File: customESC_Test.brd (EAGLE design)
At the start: 152.4 x 127 mm, 54 parts

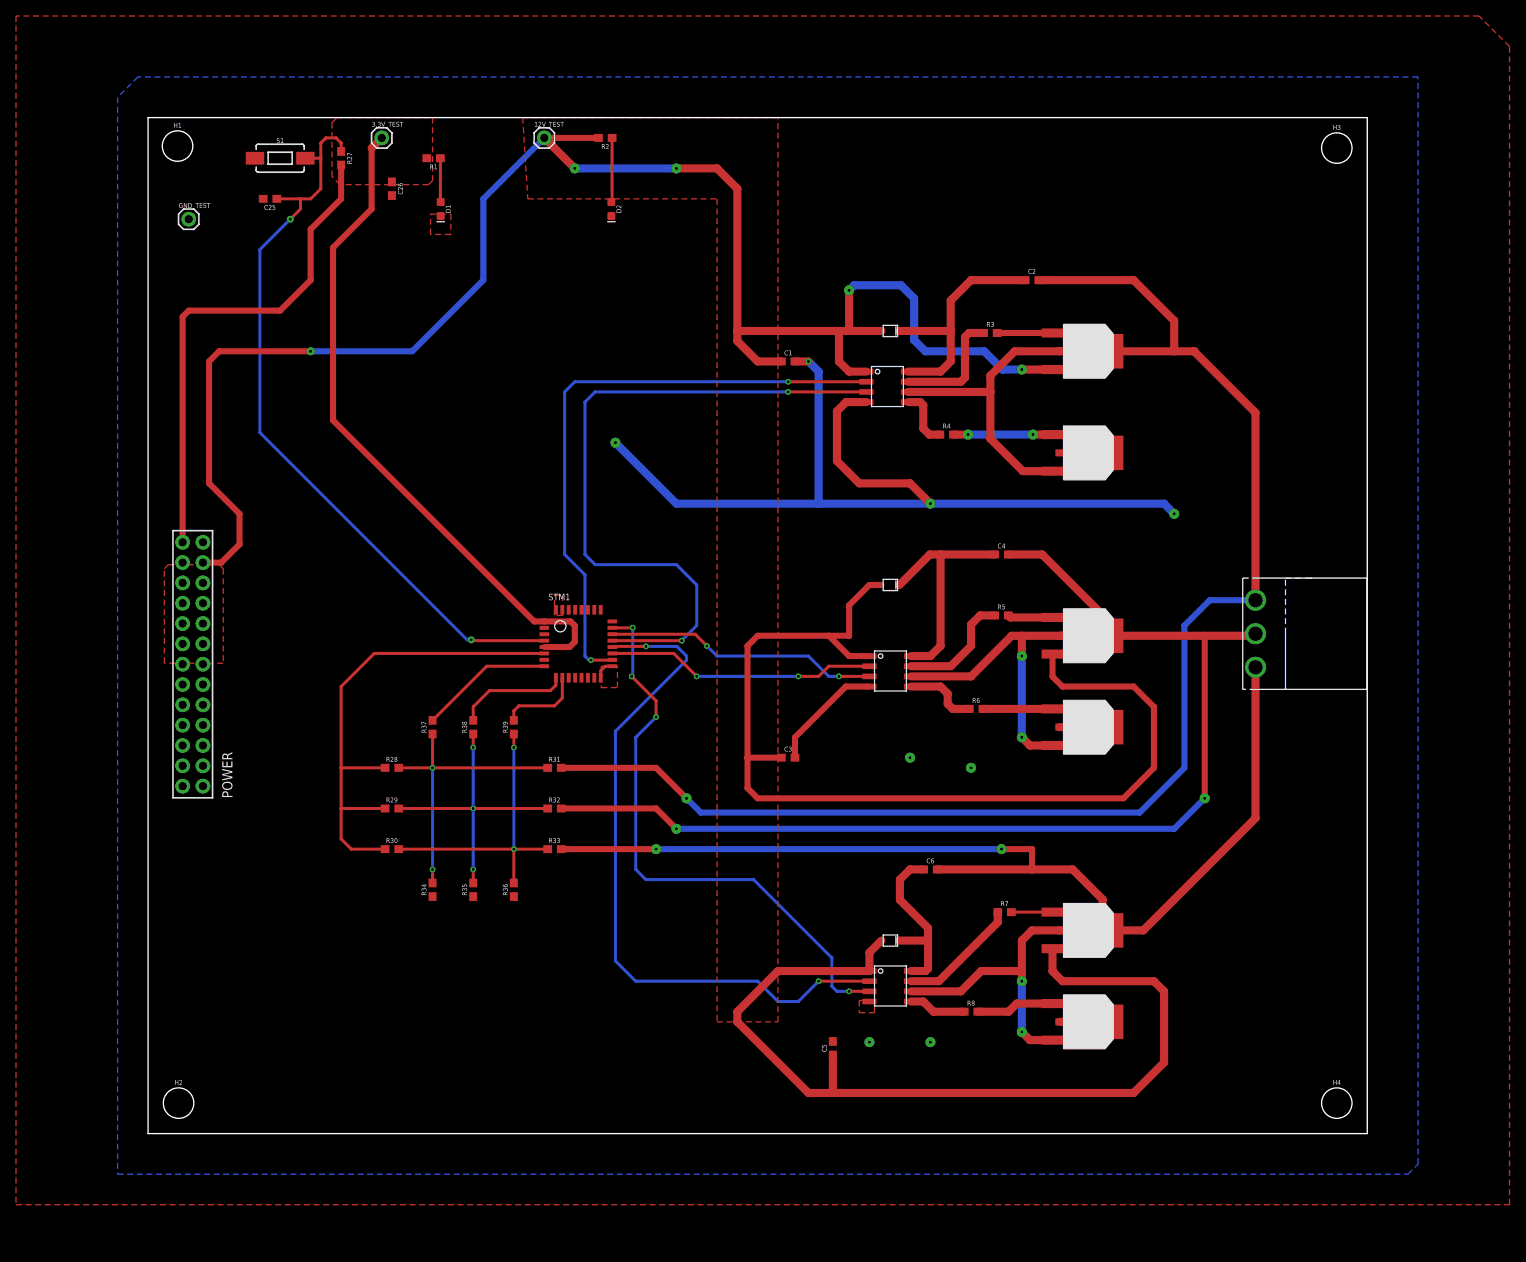
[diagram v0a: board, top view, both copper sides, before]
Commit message: added paths for input and added test leds. needs a design review
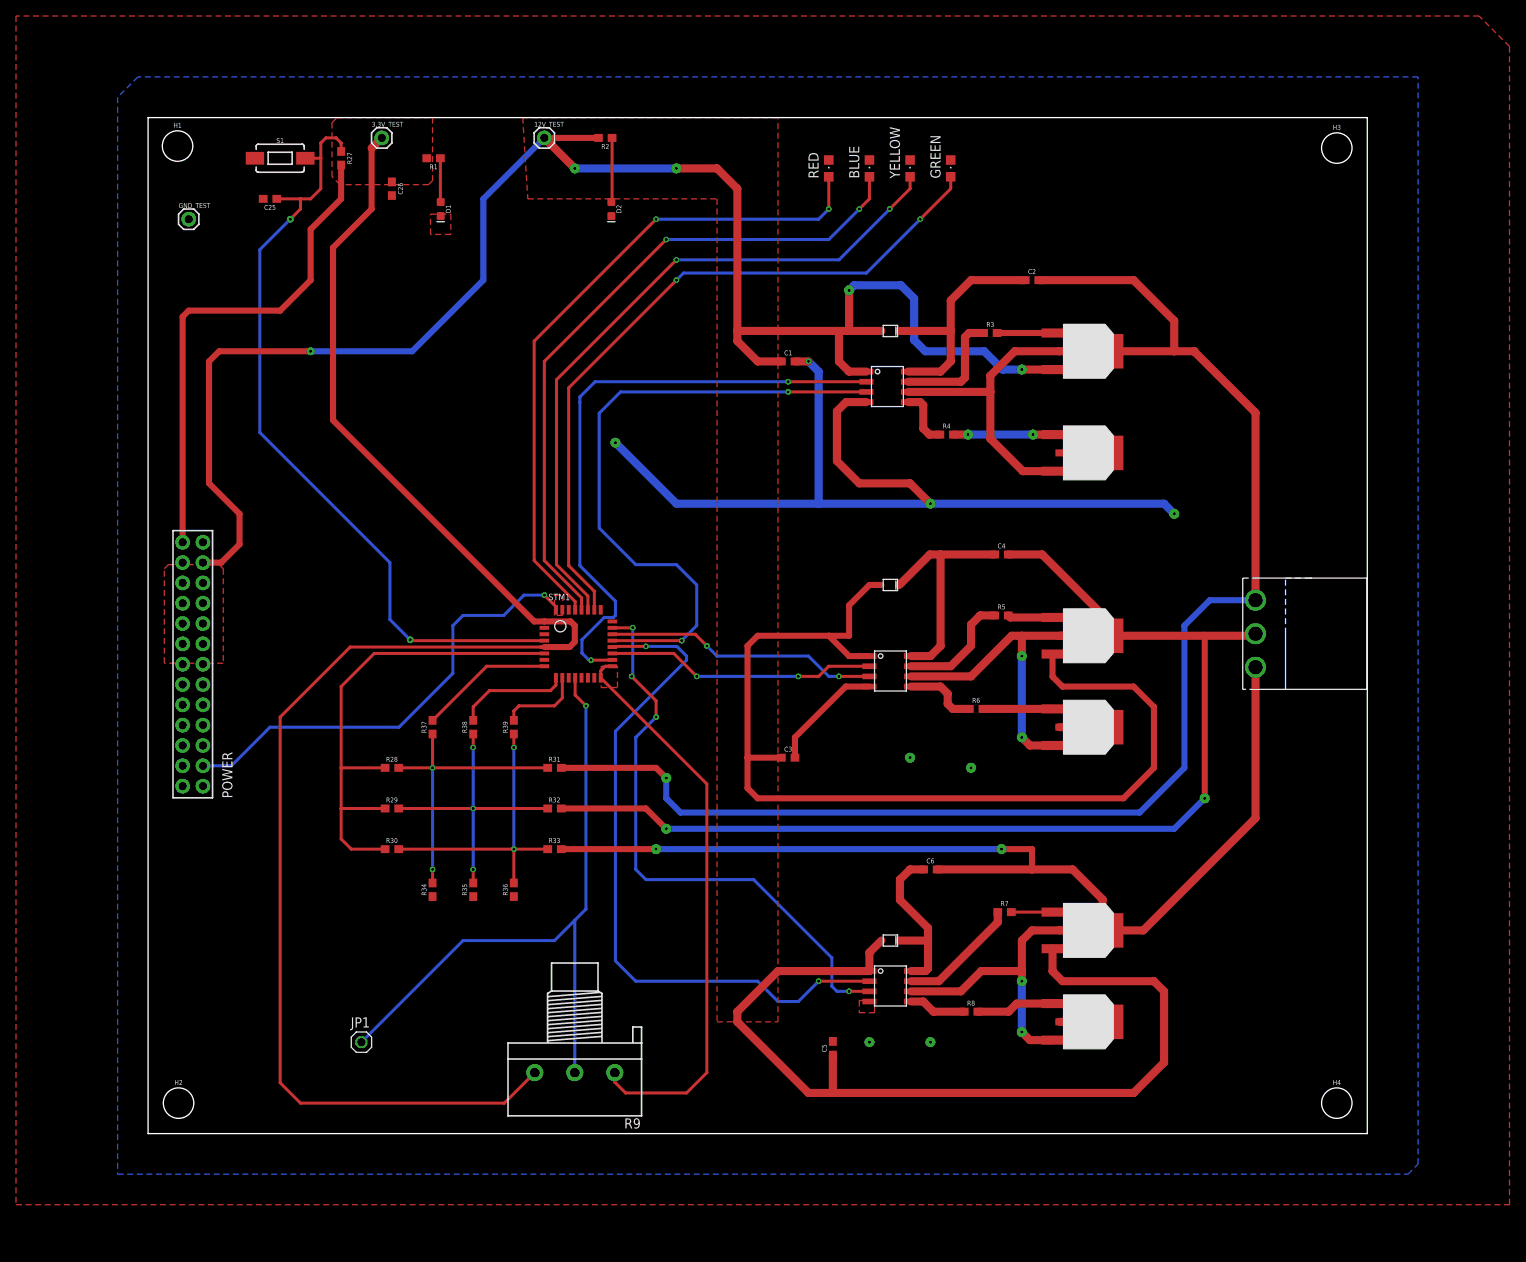
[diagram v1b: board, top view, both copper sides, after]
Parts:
- added BLUE, GREEN, RED, YELLOW: (no value), led:CHIPLED_0805
- added JP1: (no value), pinhead:1X01
- added R9: (no value), pot:3RP/1610N
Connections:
- removed net N$18: STM1.PA6
- new net PWM_IN: JP1.1, R9.2, STM1.PA6
- new net TEST_LED1: RED.A, STM1.PB6
- new net TEST_LED2: BLUE.A, STM1.PB5
- new net TEST_LED3: STM1.PB4, YELLOW.A
- new net TEST_LED4: GREEN.A, STM1.PB3
- net GND: now also BLUE.C, GREEN.C, R9.1, RED.C, YELLOW.C
- net VCC_1: now also R9.3
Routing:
- net GND: track 145.6 -> 272.2 mm, vias 8 -> 9
- net VCC_1: track 146.8 -> 263.7 mm
- net TEST_LED4: track 0.00 -> 88.6 mm, vias 0 -> 2
- net TEST_LED3: track 0.00 -> 86.0 mm, vias 0 -> 2
- net TEST_LED2: track 0.00 -> 84.8 mm, vias 0 -> 2
- net PWM_IN: track 0.00 -> 83.5 mm, vias 0 -> 1
- net TEST_LED1: track 0.00 -> 83.4 mm, vias 0 -> 2
- net AL1: track 86.7 -> 80.4 mm
- net NRST: track 95.5 -> 99.7 mm
- net PHASE_A1: track 222.1 -> 223.5 mm
- net AH1: track 76.0 -> 77.0 mm

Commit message: done
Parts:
- added J1: 3V3 -SWCLK-GND-SWDIO- NRST, X15-ESC-Controller-Parts-Library:1X05
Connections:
- new net SWCLK: J1.2, STM1.PA14
- new net SWDIO: J1.4, STM1.PA15
- net GND: now also J1.3
- net NRST: now also J1.5
- net VCC_1: now also J1.1
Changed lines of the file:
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@@
 <layer number="56" name="wert" color="7" fill="1" visible="no" active="no"/>
 <layer number="57" name="tCAD" color="7" fill="1" visible="no" active="no"/>
+<layer number="58" name="bCopper" color="7" fill="1" visible="no" active="no"/>
 <layer number="59" name="tCarbon" color="7" fill="1" visible="no" active="no"/>
 <layer number="60" name="bCarbon" color="7" fill="1" visible="no" active="no"/>
@@
 <layer number="115" name="ReferenceISLANDS" color="7" fill="1" visible="no" active="yes"/>
 <layer number="116" name="Patch_BOT" color="9" fill="4" visible="yes" active="yes"/>
+<layer number="117" name="PM_Ref" color="7" fill="1" visible="no" active="no"/>
 <layer number="118" name="Rect_Pads" color="7" fill="1" visible="no" active="yes"/>
+<layer number="119" name="PF_Ref" color="7" fill="1" visible="no" active="no"/>
+<layer number="120" name="WFL_Ref" color="7" fill="1" visible="no" active="no"/>
 <layer number="121" name="_tsilk" color="7" fill="1" visible="yes" active="yes"/>
 <layer number="122" name="_bsilk" color="7" fill="1" visible="yes" active="yes"/>
@@
 <layer number="128" name="_bValues" color="7" fill="1" visible="yes" active="yes"/>
 <layer number="129" name="Mask" color="7" fill="1" visible="yes" active="yes"/>
+<layer number="130" name="SMDSTROOK" color="7" fill="1" visible="no" active="no"/>
 <layer number="131" name="tAdjust" color="7" fill="1" visible="yes" active="yes"/>
 <layer number="132" name="bAdjust" color="7" fill="1" visible="yes" active="yes"/>
+<layer number="133" name="bottom_silk" color="7" fill="1" visible="no" active="no"/>
+<layer number="134" name="silk_top" color="7" fill="1" visible="no" active="no"/>
+<layer number="135" name="silk_bottom" color="7" fill="1" visible="no" active="no"/>
+<layer number="136" name="silktop" color="7" fill="1" visible="no" active="no"/>
+<layer number="137" name="silkbottom" color="7" fill="1" visible="no" active="no"/>
+<layer number="138" name="EEE" color="7" fill="1" visible="no" active="no"/>
+<layer number="139" name="_tKeepout" color="7" fill="1" visible="no" active="no"/>
+<layer number="140" name="mbKeepout" color="7" fill="1" visible="no" active="no"/>
+<layer number="141" name="ASSEMBLY_TOP" color="7" fill="1" visible="no" active="no"/>
+<layer number="142" name="mbRestrict" color="7" fill="1" visible="no" active="no"/>
+<layer number="143" name="PLACE_BOUND_TOP" color="7" fill="1" visible="no" active="no"/>
 <layer number="144" name="Drill_legend" color="7" fill="1" visible="yes" active="yes"/>
+<layer number="145" name="DrillLegend_01-02" color="7" fill="1" visible="no" active="no"/>
+<layer number="146" name="DrillLegend_01-15" color="7" fill="1" visible="no" active="no"/>
+<layer number="147" name="DrillLegend_01-16" color="7" fill="1" visible="no" active="no"/>
+<layer number="148" name="DrillLegend_01-20" color="7" fill="1" visible="no" active="no"/>
+<layer number="149" name="DrillLegend_02-15" color="7" fill="1" visible="no" active="no"/>
 <layer number="150" name="Notes" color="7" fill="1" visible="yes" active="yes"/>
 <layer number="151" name="HeatSink" color="7" fill="1" visible="yes" active="yes"/>
@@
 <layer number="154" name="FabDoc2" color="7" fill="1" visible="yes" active="yes"/>
 <layer number="155" name="FabDoc3" color="7" fill="1" visible="yes" active="yes"/>
+<layer number="156" name="gesam-Maß" color="7" fill="1" visible="no" active="no"/>
+<layer number="157" name="FaceMchng" color="7" fill="1" visible="no" active="no"/>
+<layer number="158" name="FaceMMeas" color="7" fill="1" visible="no" active="no"/>
+<layer number="159" name="Geh-Bear2" color="7" fill="1" visible="no" active="no"/>
+<layer number="160" name="Topologie" color="7" fill="1" visible="no" active="no"/>
+<layer number="161" name="tomplace2" color="7" fill="1" visible="no" active="no"/>
+<layer number="166" name="AntennaArea" color="7" fill="1" visible="no" active="no"/>
+<layer number="168" name="4mmHeightArea" color="7" fill="1" visible="no" active="no"/>
+<layer number="191" name="mNets" color="7" fill="1" visible="no" active="no"/>
+<layer number="192" name="mBusses" color="7" fill="1" visible="no" active="no"/>
+<layer number="193" name="mPins" color="7" fill="1" visible="no" active="no"/>
+<layer number="194" name="mSymbols" color="7" fill="1" visible="no" active="no"/>
+<layer number="195" name="mNames" color="7" fill="1" visible="no" active="no"/>
+<layer number="196" name="mValues" color="7" fill="1" visible="no" active="no"/>
 <layer number="199" name="Contour" color="7" fill="1" visible="yes" active="yes"/>
 <layer number="200" name="200bmp" color="1" fill="10" visible="yes" active="yes"/>
@@
 <layer number="250" name="Descript" color="3" fill="1" visible="no" active="no"/>
 <layer number="251" name="SMDround" color="12" fill="11" visible="no" active="no"/>
+<layer number="252" name="BR-BS" color="7" fill="1" visible="no" active="no"/>
+<layer number="253" name="Extra" color="7" fill="1" visible="no" active="no"/>
 <layer number="254" name="cooling" color="7" fill="1" visible="yes" active="yes"/>
 <layer number="255" name="routoute" color="7" fill="1" visible="yes" active="yes"/>
@@
 <attribute name="VALUE" x="102.87" y="119.38" size="1.27" layer="27" rot="R90"/>
 </element>
+<element name="J1" library="X15-ESC-Controller-Parts-Library" package="1X05" value="3V3 -SWCLK-GND-SWDIO- NRST" x="-13.97" y="-11.43" smashed="yes">
+<attribute name="NAME" x="-15.24" y="-10.033" size="0.6096" layer="25" font="vector" ratio="20"/>
+<attribute name="VALUE" x="-15.494" y="-13.716" size="0.6096" layer="25"/>
+</element>
 </elements>
 <signals>
@@
 <wire x1="16.51" y1="52.07" x2="25.26" y2="60.82" width="0.381" layer="1"/>
 <wire x1="25.26" y1="60.82" x2="49.53" y2="60.82" width="0.381" layer="1"/>
+<contactref element="J1" pad="1"/>
+<wire x1="30.48" y1="118.96" x2="34.837" y2="121.92" width="0" layer="19" extent="1-1"/>
+<wire x1="29.21" y1="124.46" x2="30.48" y2="118.96" width="0" layer="19" extent="1-1"/>
+<wire x1="24.13" y1="121.07" x2="29.21" y2="124.46" width="0" layer="19" extent="1-1"/>
+<wire x1="-13.97" y1="-11.43" x2="48.34" y2="7.62" width="0" layer="19" extent="1-1"/>
 </signal>
 <signal name="VCC_2">
@@
 <wire x1="46.99" y1="67.31" x2="44.45" y2="64.77" width="0.381" layer="16"/>
 <wire x1="39.37" y1="64.77" x2="44.45" y2="64.77" width="0.381" layer="16"/>
+<contactref element="J1" pad="3"/>
+<wire x1="4.318" y1="43.434" x2="-8.89" y2="-11.43" width="0" layer="19" extent="1-1"/>
 </signal>
 <signal name="PHASE_A1">
@@
 <wire x1="21.59" y1="121.92" x2="21.59" y2="118.11" width="0.381" layer="1"/>
 <wire x1="19.66" y1="121.92" x2="21.59" y2="121.92" width="0.381" layer="1"/>
+<contactref element="J1" pad="5"/>
+<wire x1="-3.81" y1="-11.43" x2="32.766" y2="61.722" width="0" layer="19" extent="1-1"/>
 </signal>
 <signal name="COM1">
@@
 <wire x1="53.38" y1="66.508" x2="48.26" y2="71.628" width="0.381" layer="1"/>
 </signal>
+<signal name="SWDIO">
+<contactref element="J1" pad="4"/>
+<contactref element="STM1" pad="PA15"/>
+<wire x1="-6.35" y1="-11.43" x2="56.58" y2="65.47" width="0" layer="19" extent="1-1"/>
+</signal>
+<signal name="SWCLK">
+<contactref element="J1" pad="2"/>
+<contactref element="STM1" pad="PA14"/>
+<wire x1="-11.43" y1="-11.43" x2="58.03" y2="64.02" width="0" layer="19" extent="1-1"/>
+</signal>
 </signals>
